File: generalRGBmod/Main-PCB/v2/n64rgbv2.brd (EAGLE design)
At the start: 50.5 x 31.1 mm, 76 parts, among them J3 2510-, U1 5M570ZT100C5, U2 ADV7125/ADV7123, U4 TLV70018-DDC

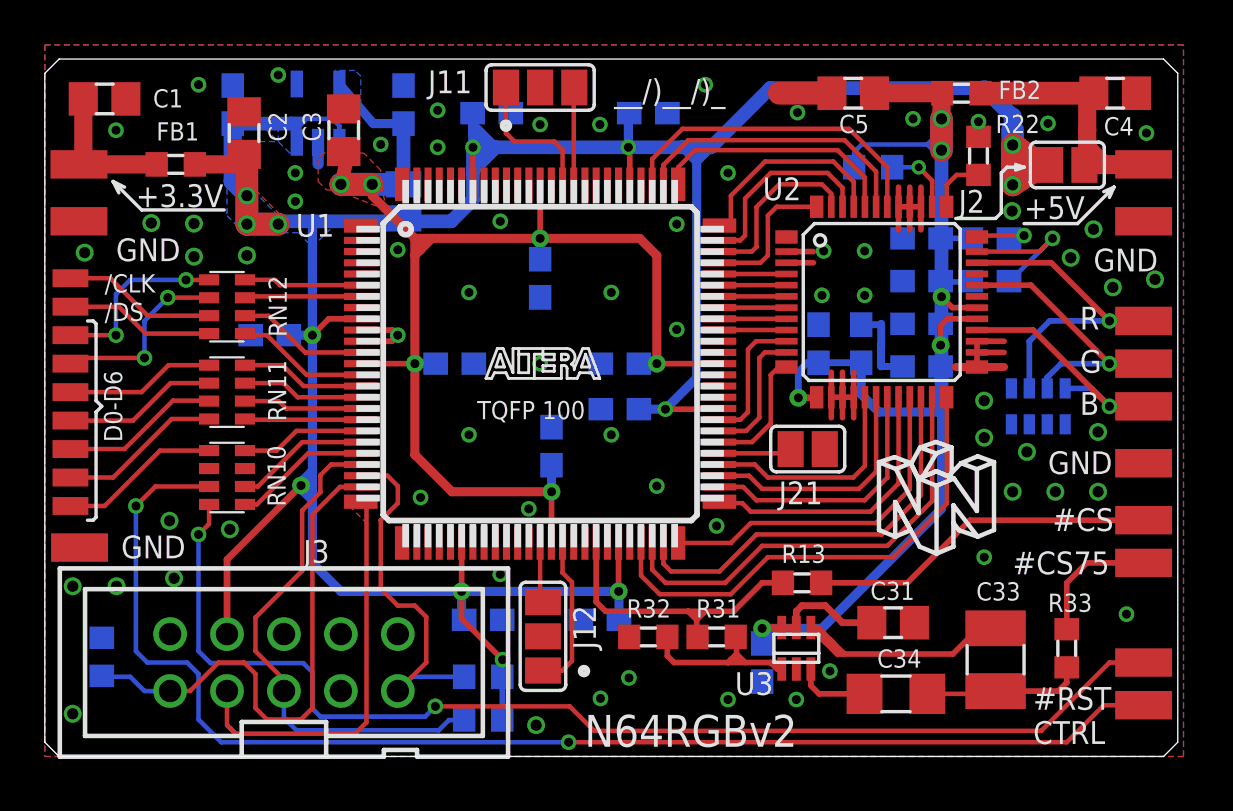
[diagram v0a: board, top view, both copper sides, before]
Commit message: use LSB of the ADV7125 (new design is compatible to initial public N64RGBv2 Version 20171211)
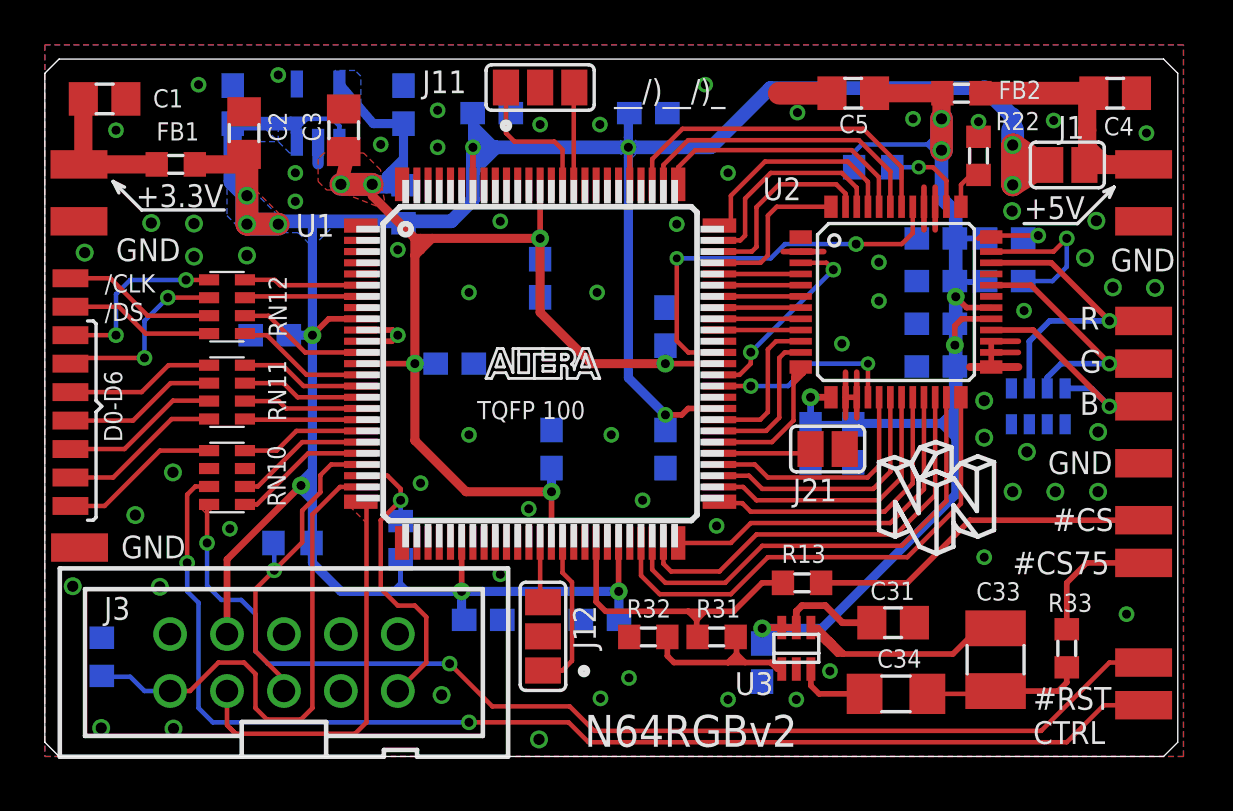
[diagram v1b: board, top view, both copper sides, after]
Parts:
- removed J1: (no value), jumper:SJ
- added FB3: (no value), rcl:R0603
- moved R11 11.6 mm to (11.0, 9.53)
- moved R12 7.12 mm to (15.9, 9.65), turned to 90 degrees
- moved C20 4.46 mm to (36.1, 14.0), turned to 270 degrees
- moved C21 4.46 mm to (34.2, 14.0), turned to 270 degrees
- moved C17 2.70 mm to (27.7, 13.7), turned to 270 degrees
- moved C12 2.62 mm to (27.7, 19.2), turned to 90 degrees
- moved J21 0.89 mm to (34.9, 13.7)
- moved C22 0.63 mm to (39.8, 19.3)
- moved C23 0.63 mm to (39.8, 17.4)
- moved C24 0.63 mm to (39.8, 21.2)
- moved C25 0.63 mm to (39.8, 23.1)
- moved C27 0.63 mm to (42.8, 23.1)
- moved C28 0.63 mm to (42.8, 21.2)
- moved U2 0.63 mm to (38.0, 20.3)
- moved C11 0.13 mm to (22.6, 13.7)
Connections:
- new net N$25: U1.64, U2.41
- new net N$41: U1.62, U2.3
- new net N$43: U1.61, U2.16
- net GND: no longer U2.16, U2.3, U2.41
- net VCC@1.8V: now also FB3.2; no longer J1.2
- net VCC@3.3V: now also FB3.1; no longer J1.1
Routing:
- net N$25: track 0.00 -> 18.0 mm, vias 0 -> 2
- net GND: track 32.8 -> 23.3 mm
- net N$41: track 0.00 -> 8.91 mm, vias 0 -> 2
- net N$43: track 0.00 -> 8.70 mm, vias 0 -> 2
- net TMS: track 23.0 -> 14.6 mm, vias 0 -> 1
- net VCC@3.3V: track 152.9 -> 147.3 mm, vias 13 -> 12
- net N$6: track 58.6 -> 54.3 mm
- net N$5: track 53.0 -> 50.4 mm
- net N$32: track 5.64 -> 8.06 mm
- net TDI: track 16.3 -> 14.1 mm, vias 0 -> 1
- net VCC@1.8V: track 65.8 -> 63.8 mm
- net +5V: track 68.2 -> 69.4 mm
- net N$88: track 2.90 -> 4.03 mm
- net RGSB: track 3.25 -> 4.10 mm
- net N$63: track 6.35 -> 7.09 mm
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- added copper zone on layer 1, net N$5
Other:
- board text added: "FB3"
- board text added: "N64RGB2_20171219"
- board text removed: "J2"
- board text removed: "N64RGB2_20171211"

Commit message: N64RGBv1/v2 misc updates  (thanks to iFixRetro for giving feedback here!!!): - bugfix BOM and silkscreen (N64RGBv2) - silkscreen update to distinguish between MaxII and MaxV setup avoiding assembly mistakes - move power regulator to BOT copper side (N64RGBv1) - additional jumper J1 to select between 240LE and 570LE CPLD (for proper usage of the 5M240ZT)
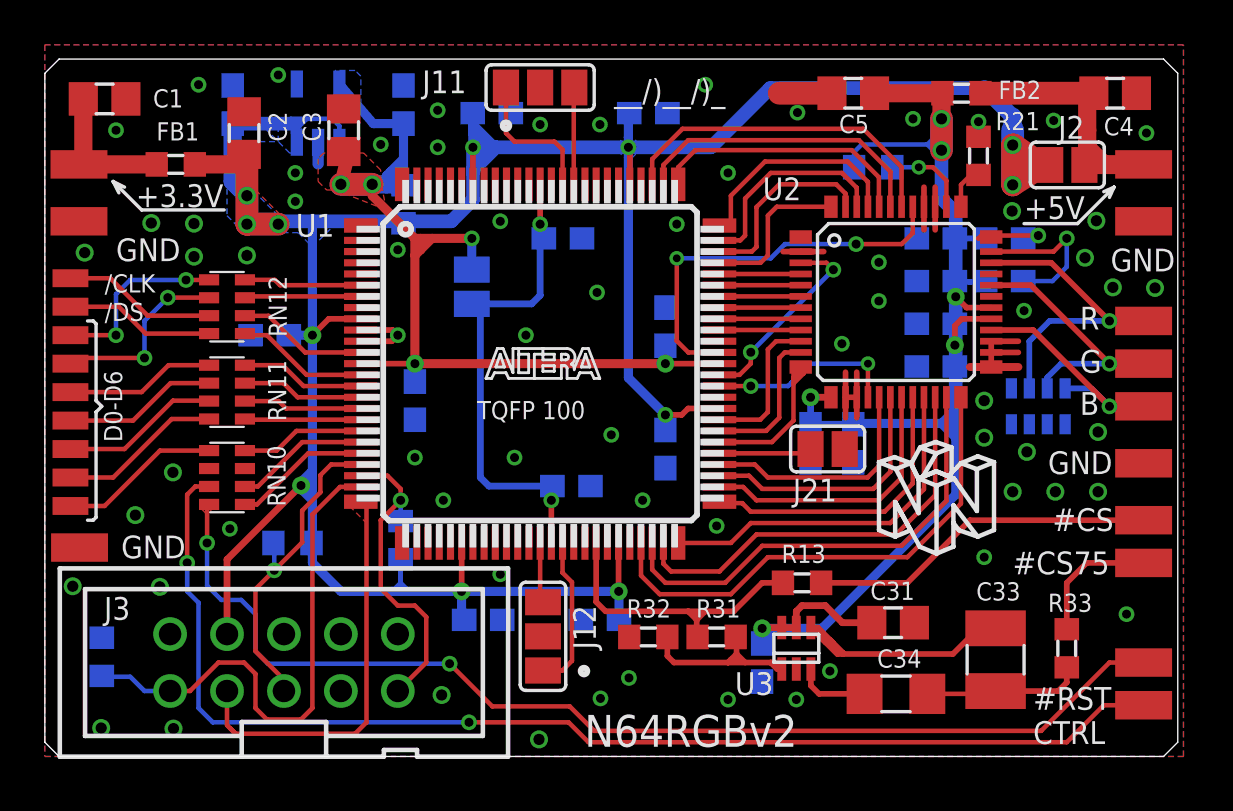
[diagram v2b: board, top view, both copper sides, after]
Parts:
- added J1: (no value), jumper:SJ
- moved C10 2.43 mm to (16.5, 15.9), turned to 270 degrees
- moved C13 2.05 mm to (23.1, 23.1), turned to 180 degrees
- moved C11 1.88 mm to (23.5, 12.1), turned to 180 degrees
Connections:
- new net VCCINT: C11.1, C13.1, J1.2, U1.39, U1.88
- net VCC@1.8V: now also J1.1; no longer C11.1, C13.1, U1.39, U1.88
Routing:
- net VCCINT: track 0.00 -> 22.2 mm, vias 0 -> 2
- net VCC@1.8V: track 63.8 -> 46.3 mm, vias 6 -> 5
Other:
- board text added: "(570LEs)"
- board text added: "Don't use U4,C41,C42 Don't use FB3!!!"
- board text added: "J2"
- board text added: "MaxII: MaxV:"
- board text added: "N64RGBv2_20180121"
- board text removed: "N64RGB2_20171219"
